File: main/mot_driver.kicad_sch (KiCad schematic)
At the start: 0 parts

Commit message: [PSU] Compute values for LT8710 PSU
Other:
- company: (none) -> Julien FAUCHER
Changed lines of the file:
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@@
 (kicad_sch (version 20230819) (generator eeschema)
   (paper "A4")
+  (title_block
+    (date "2023-04-05")
+    (rev "0.1")
+    (company "Julien FAUCHER")
+    (comment 1 "Defis solaires 2024")
+  )
   (sheet (at 67.31 36.83) (size 67.31 13.97) (fields_autoplaced)
     (stroke (width 0.1524) (type solid))

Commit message: PSU should be OK
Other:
- added sheet Phase B Driver (phase_driver.kicad_sch)
- added sheet Phase C Driver (phase_driver.kicad_sch)
- sheet Phase A Driver ports: added INH, INL, OUT; removed none

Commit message: Progresses
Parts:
- added D301, D302, D303: RED, symbol Device:LED
- added D304, D305, D306: BLUE, symbol Device:LED
- added Q301: Q_NMOS_GDS, symbol Device:Q_NMOS_GDS
- added R301, R302, R303, R304, R305, R306: 3k3, symbol Device:R
- added R307: 100k, symbol Device:R
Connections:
- net MOT_DRIVE.AH: now also R301.1
- net MOT_DRIVE.AL: now also R304.1
- net MOT_DRIVE.BH: now also R302.1
- net MOT_DRIVE.BL: now also R305.1
- net MOT_DRIVE.CH: now also R303.1
- net MOT_DRIVE.CL: now also R306.1
- new net: D301.1 (K), D302.1 (K), D303.1 (K), D304.1 (K), D305.1 (K), D306.1 (K), Q301.2 (D)
- new net: D303.2 (A), R303.2
- new net: D301.2 (A), R301.2
- new net: D306.2 (A), R306.2
- new net: D302.2 (A), R302.2
- new net: D304.2 (A), R304.2
- new net: D305.2 (A), R305.2
- new net GNDD: Q301.3 (S), R307.2
- new net LED_EN: Q301.1 (G), R307.1
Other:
- note added: "Any high value to avoid floating gate while not wasting power."

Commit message: Update schematics
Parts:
- removed D301, D302, D303: RED, symbol Device:LED
- removed D304, D305, D306: BLUE, symbol Device:LED
- removed Q301: Q_NMOS_GDS, symbol Device:Q_NMOS_GDS
- removed R301, R302, R303, R304, R305, R306: 3k3, symbol Device:R
- removed R307: 100k, symbol Device:R
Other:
- note removed: "Any high value to avoid floating gate while not wasting power."

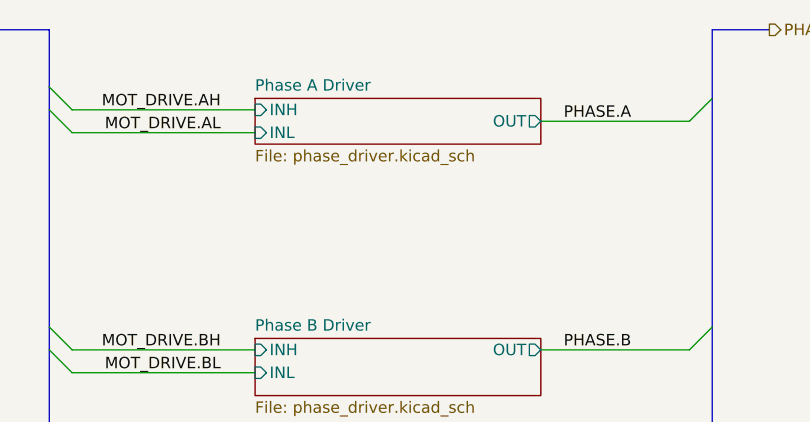
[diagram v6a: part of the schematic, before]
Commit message: Finalize sch and start component mapping
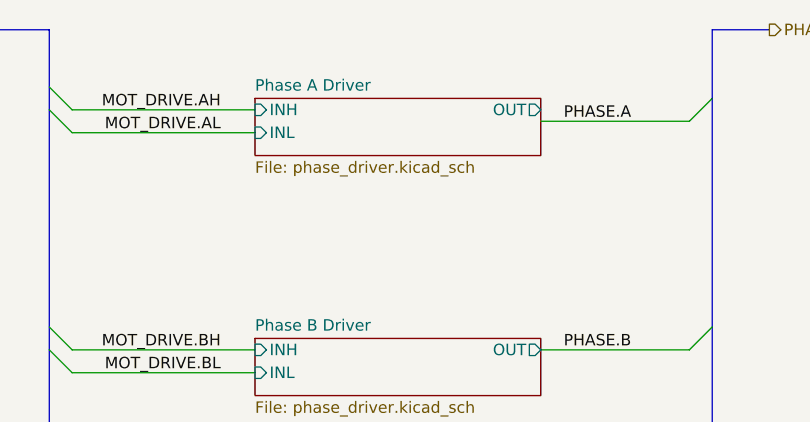
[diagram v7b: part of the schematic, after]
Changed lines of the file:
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@@
 	(sheet
 		(at 114.3 38.1)
-		(size 31.75 5.08)
+		(size 31.75 6.35)
 		(fields_autoplaced yes)
 		(stroke
@@
 		)
 		(property "Sheetfile" "phase_driver.kicad_sch"
-			(at 114.3 43.7646 0)
+			(at 114.3 45.0346 0)
 			(effects
 				(font
@@
 		)
 		(pin "OUT" output
-			(at 146.05 40.64 0)
+			(at 146.05 39.37 0)
 			(effects
 				(font
@@
 			(project "dsv4"
 				(path "/c07e9297-fde8-4755-803e-d05072cd6096/5b9a617b-6d93-4d9f-bce1-510d294da22c"
-					(page "4")
+					(page "9")
 				)
 				(path "/c07e9297-fde8-4755-803e-d05072cd6096/bed5353e-e607-4c1c-98ea-22040242af2e"
-					(page "9")
+					(page "18")
 				)
 			)

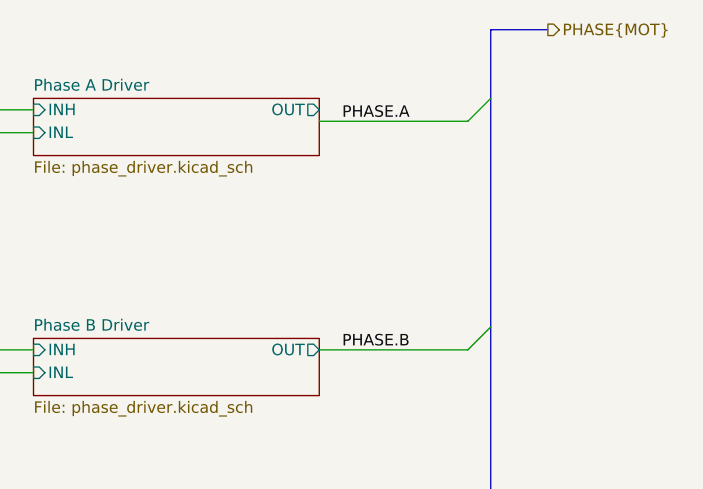
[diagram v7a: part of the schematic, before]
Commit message: Power routed
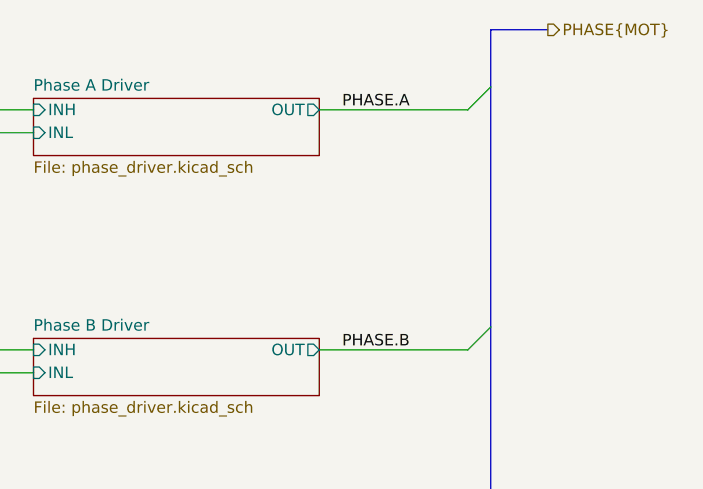
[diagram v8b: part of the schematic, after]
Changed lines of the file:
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@@
 	)
 	(bus_entry
-		(at 165.1 38.1)
+		(at 165.1 36.83)
 		(size -2.54 2.54)
 		(stroke
@@
 	(bus
 		(pts
-			(xy 165.1 38.1) (xy 165.1 63.5)
-		)
-		(stroke
-			(width 0)
-			(type default)
-		)
-	)
-	(bus
-		(pts
-			(xy 165.1 30.48) (xy 165.1 38.1)
+			(xy 165.1 30.48) (xy 165.1 36.83)
 		)
 		(stroke
@@
 		)
 	)
-	(wire
-		(pts
-			(xy 146.05 40.64) (xy 162.56 40.64)
+	(bus
+		(pts
+			(xy 165.1 36.83) (xy 165.1 63.5)
+		)
+		(stroke
+			(width 0)
+			(type default)
+		)
+	)
+	(wire
+		(pts
+			(xy 146.05 39.37) (xy 162.56 39.37)
 		)
 		(stroke
@@
 	)
 	(label "PHASE.A"
-		(at 148.59 40.64 0)
-		(fields_autoplaced yes)
-		(effects
+		(at 148.59 39.37 0)
+		(fields_autoplaced yes)
+		(effects
